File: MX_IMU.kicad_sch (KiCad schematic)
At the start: 31 parts, among them SW1 SW_SPST, U1 ld39150dt33-r, U200 STM32F405RGT6, U4 AT24C256, Y200 16MHz

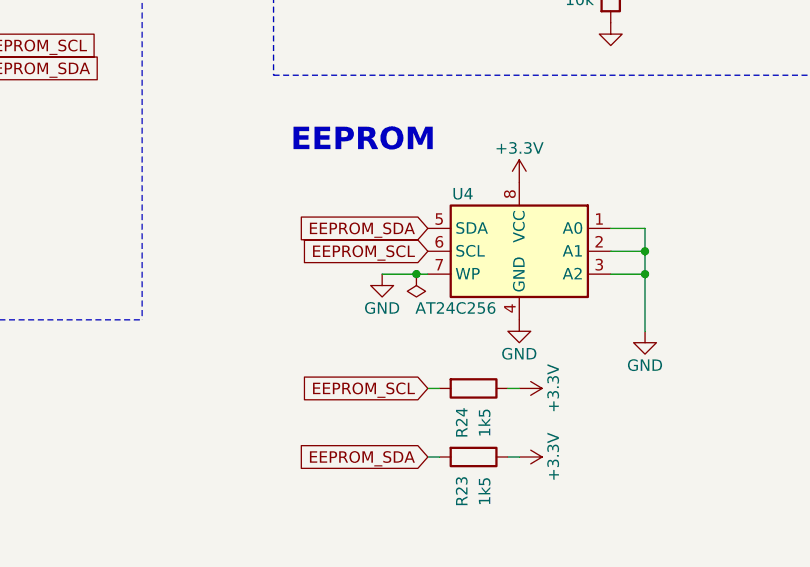
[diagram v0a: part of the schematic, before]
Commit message: add usb and clean up
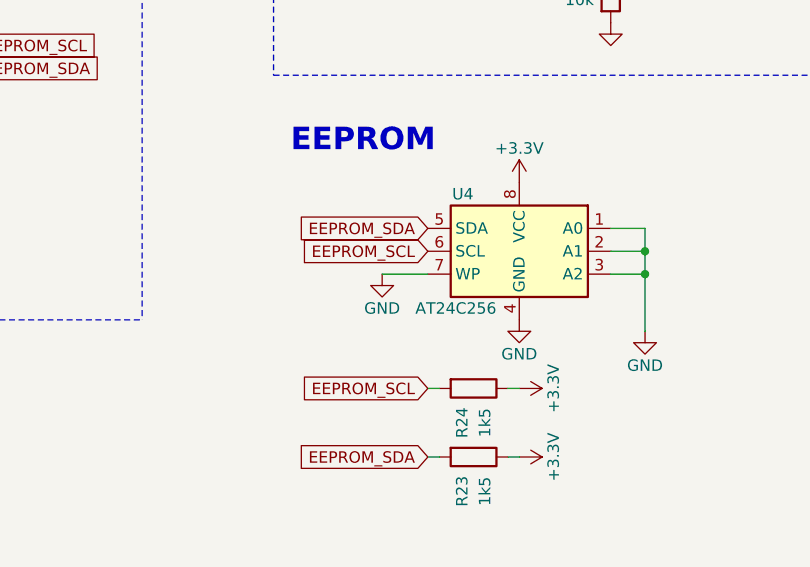
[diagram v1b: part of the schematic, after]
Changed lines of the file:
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@@
 	)
 	(junction
-		(at 151.13 152.4)
-		(diameter 0)
-		(color 0 0 0 0)
-	)
-	(junction
 		(at 69.85 25.4)
 		(diameter 0)
@@
 	(wire
 		(pts
-			(xy 151.13 152.4) (xy 152.4 152.4)
+			(xy 147.32 152.4) (xy 152.4 152.4)
 		)
 		(stroke
@@
 	(wire
 		(pts
-			(xy 147.32 152.4) (xy 151.13 152.4)
-		)
-		(stroke
-			(width 0)
-			(type default)
-		)
-	)
-	(wire
-		(pts
 			(xy 152.4 165.1) (xy 153.67 165.1)
 		)
@@
 			)
 		)
-		(property "Description" ""
+		(property "Description" "Resistor, small symbol"
 			(at 165.1 58.42 0)
 			(effects
@@
 					(size 1.27 1.27)
 				)
+				(hide yes)
 			)
 		)
@@
 					(size 1.27 1.27)
 				)
+				(hide yes)
 			)
 		)
@@
 					(unit 1)
 				)
-			)
-		)
-	)
-	(symbol
-		(lib_id "power:PWR_FLAG")
-		(at 151.13 152.4 180)
-		(unit 1)
-		(exclude_from_sim no)
-		(in_bom yes)
-		(on_board yes)
-		(dnp no)
-		(fields_autoplaced yes)
-		(property "Reference" "#FLG03"
-			(at 151.13 154.305 0)
-			(effects
-				(font
-					(size 1.27 1.27)
-				)
-				(hide yes)
-			)
-		)
-		(property "Value" "PWR_FLAG"
-			(at 151.13 156.972 0)
-			(effects
-				(font
-					(size 1.27 1.27)
-				)
-				(hide yes)
-			)
-		)
-		(property "Footprint" ""
-			(at 151.13 152.4 0)
-			(effects
-				(font
-					(size 1.27 1.27)
-				)
-				(hide yes)
-			)
-		)
-		(property "Datasheet" "~"
-			(at 151.13 152.4 0)
-			(effects
-				(font
-					(size 1.27 1.27)
-				)
-				(hide yes)
-			)
-		)
-		(property "Description" "Special symbol for telling ERC where power comes from"
-			(at 151.13 152.4 0)
-			(effects
-				(font
-					(size 1.27 1.27)
-				)
-				(hide yes)
-			)
-		)
-		(pin "1"
-		)
-		(instances
-			(project ""
-				(path "/8ed38441-7d4e-4e89-870f-07e11c6dce38"
-					(reference "#FLG03")
-					(unit 1)
-				)

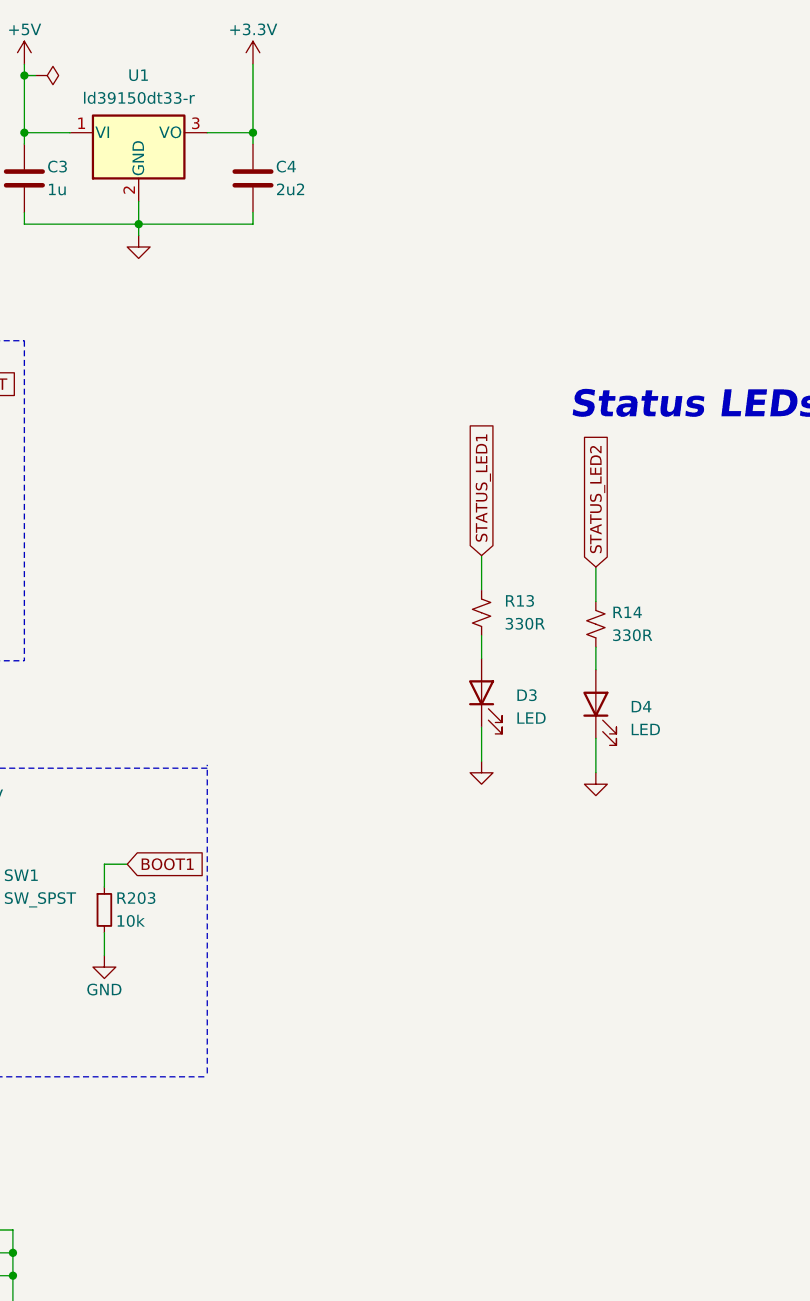
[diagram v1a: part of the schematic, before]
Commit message: add mounting hole
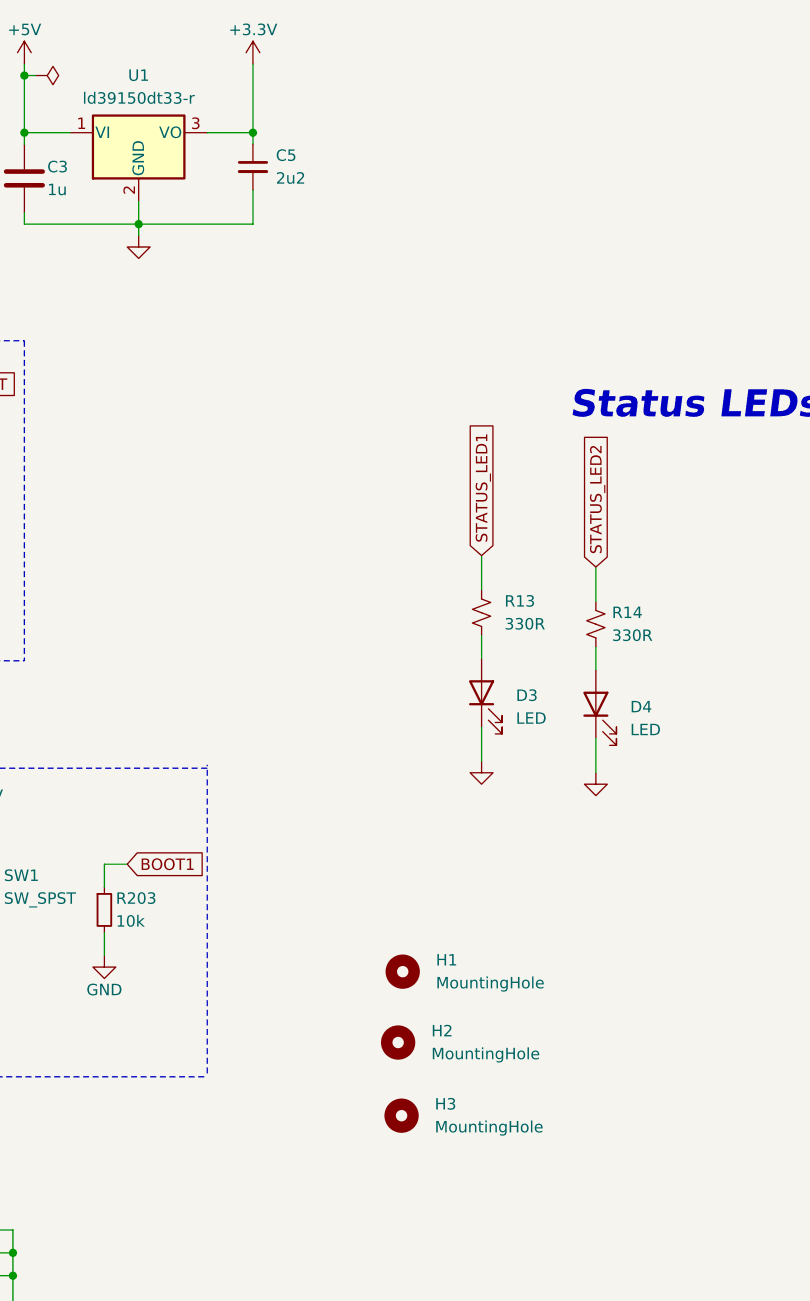
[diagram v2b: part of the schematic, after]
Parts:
- removed C4: 2u2, Capacitor_SMD:C_0603_1608Metric, symbol Device:C
- added C5: 2u2, Capacitor_SMD:C_0603_1608Metric, symbol Device:C_Small
- added H1, H2, H3: MountingHole, MountingHole:MountingHole_2mm, symbol Mechanical:MountingHole
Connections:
- net +3.3V: now also C5.1
- net GND: now also C5.2
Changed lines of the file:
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@@
 	(wire
 		(pts
-			(xy 203.2 35.56) (xy 203.2 34.29)
+			(xy 203.2 31.75) (xy 203.2 35.56)
 		)
 		(stroke
@@
 	)
 	(symbol
-		(lib_id "Device:C")
-		(at 203.2 30.48 0)
+		(lib_id "Mechanical:MountingHole")
+		(at 219.71 134.62 0)
 		(unit 1)
 		(exclude_from_sim no)
-		(in_bom yes)
+		(in_bom no)
 		(on_board yes)
 		(dnp no)
-		(property "Reference" "C4"
-			(at 205.74 29.21 0)
+		(fields_autoplaced yes)
+		(property "Reference" "H3"
+			(at 223.393 133.3499 0)
 			(effects
 				(font
@@
 			)
 		)
-		(property "Value" "2u2"
-			(at 205.74 31.75 0)
+		(property "Value" "MountingHole"
+			(at 223.393 135.8899 0)
 			(effects
 				(font
@@
 			)
 		)
-		(property "Footprint" "Capacitor_SMD:C_0603_1608Metric"
-			(at 204.1652 34.29 0)
+		(property "Footprint" "MountingHole:MountingHole_2mm"
+			(at 219.71 134.62 0)
 			(effects
 				(font
@@
 		)
 		(property "Datasheet" "~"
-			(at 203.2 30.48 0)
+			(at 219.71 134.62 0)
 			(effects
 				(font
@@
 			)
 		)
-		(property "Description" "Unpolarized capacitor"
-			(at 203.2 30.48 0)
+		(property "Description" "Mounting Hole without connection"
+			(at 219.71 134.62 0)
 			(effects
 				(font
@@
 			)
 		)
-		(pin "1"
-		)
-		(pin "2"
-		)
 		(instances
 			(project "MX_IMU"
 				(path "/8ed38441-7d4e-4e89-870f-07e11c6dce38"
-					(reference "C4")
+					(reference "H3")
 					(unit 1)
 				)
@@
 	)
 	(symbol
+		(lib_id "Device:C_Small")
+		(at 203.2 29.21 0)
+		(unit 1)
+		(exclude_from_sim no)
+		(in_bom yes)
+		(on_board yes)
+		(dnp no)
+		(property "Reference" "C5"
+			(at 205.74 27.94 0)
+			(effects
+				(font
+					(size 1.27 1.27)
+				)
+				(justify left)
+			)
+		)
+		(property "Value" "2u2"
+			(at 205.74 30.48 0)
+			(effects
+				(font
+					(size 1.27 1.27)
+				)
+				(justify left)
+			)
+		)
+		(property "Footprint" "Capacitor_SMD:C_0603_1608Metric"
+			(at 203.2 29.21 0)
+			(effects
+				(font
+					(size 1.27 1.27)
+				)
+				(hide yes)
+			)
+		)
+		(property "Datasheet" "~"
+			(at 203.2 29.21 0)
+			(effects
+				(font
+					(size 1.27 1.27)
+				)
+				(hide yes)
+			)
+		)
+		(property "Description" ""
+			(at 203.2 29.21 0)
+			(effects
+				(font
+					(size 1.27 1.27)
+				)
+			)
+		)
+		(property "LCSC Part #" "C23630"
+			(at 203.2 29.21 0)
+			(effects
+				(font
+					(size 1.27 1.27)
+				)
+				(hide yes)
+			)
+		)
+		(pin "1"
+		)
+		(pin "2"
+		)
+		(instances
+			(project "MX_IMU"
+				(path "/8ed38441-7d4e-4e89-870f-07e11c6dce38"
+					(reference "C5")
+					(unit 1)
+				)
+			)
+		)
+	)
+	(symbol
 		(lib_id "power:+3.3V")
 		(at 266.7 63.5 0)
@@
 	)
 	(symbol
+		(lib_id "Mechanical:MountingHole")
+		(at 219.329 126.492 0)
+		(unit 1)
+		(exclude_from_sim no)
+		(in_bom no)
+		(on_board yes)
+		(dnp no)
+		(fields_autoplaced yes)
+		(property "Reference" "H2"
+			(at 223.012 125.2219 0)
+			(effects
+				(font
+					(size 1.27 1.27)
+				)
+				(justify left)
+			)
+		)
+		(property "Value" "MountingHole"
+			(at 223.012 127.7619 0)
+			(effects
+				(font
+					(size 1.27 1.27)
+				)
+				(justify left)
+			)
+		)
+		(property "Footprint" "MountingHole:MountingHole_2mm"
+			(at 219.329 126.492 0)
+			(effects
+				(font
+					(size 1.27 1.27)
+				)
+				(hide yes)
+			)
+		)
+		(property "Datasheet" "~"
+			(at 219.329 126.492 0)
+			(effects
+				(font
+					(size 1.27 1.27)
+				)
+				(hide yes)
+			)
+		)
+		(property "Description" "Mounting Hole without connection"
+			(at 219.329 126.492 0)
+			(effects
+				(font
+					(size 1.27 1.27)
+				)
+				(hide yes)
+			)
+		)
+		(instances
+			(project "MX_IMU"
+				(path "/8ed38441-7d4e-4e89-870f-07e11c6dce38"
+					(reference "H2")
+					(unit 1)
+				)
+			)
+		)
+	)
+	(symbol
 		(lib_id "power:+3.3V")
 		(at 162.56 142.24 0)
@@
 					(unit 1)
 				)
+			)
+		)
+	)
+	(symbol
+		(lib_id "Mechanical:MountingHole")
+		(at 219.837 118.618 0)
+		(unit 1)
+		(exclude_from_sim no)
+		(in_bom no)
+		(on_board yes)
+		(dnp no)
+		(fields_autoplaced yes)
+		(property "Reference" "H1"
+			(at 223.52 117.3479 0)
+			(effects
+				(font
+					(size 1.27 1.27)
+				)
+				(justify left)
+			)
+		)
+		(property "Value" "MountingHole"
+			(at 223.52 119.8879 0)
+			(effects
+				(font
+					(size 1.27 1.27)
+				)
+				(justify left)
+			)
+		)
+		(property "Footprint" "MountingHole:MountingHole_2mm"
+			(at 219.837 118.618 0)
+			(effects
+				(font
+					(size 1.27 1.27)
+				)
+				(hide yes)
+			)
+		)
+		(property "Datasheet" "~"
+			(at 219.837 118.618 0)
+			(effects
+				(font
+					(size 1.27 1.27)
+				)
+				(hide yes)
+			)
+		)
+		(property "Description" "Mounting Hole without connection"
+			(at 219.837 118.618 0)
+			(effects
+				(font
+					(size 1.27 1.27)
+				)
+				(hide yes)
+			)
+		)
+		(instances
+			(project ""
+				(path "/8ed38441-7d4e-4e89-870f-07e11c6dce38"
+					(reference "H1")
+					(unit 1)
+				)

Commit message: Cleanup and check on JCLPCB
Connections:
- net SWO: no longer names the net of U200.55 (PB3)
- no-connect marks 32 -> 33
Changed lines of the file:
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@@
+	)
+	(no_connect
+		(at 104.14 114.3)
 	)
 	(no_connect
@@
 			(effects
 				(font
-					(size 1.27 1.27)
-				)
-				(hide yes)
-			)
-		)
-	)
-	(global_label "SWO"
-		(shape input)
-		(at 104.14 114.3 0)
-		(effects
-			(font
-				(size 1.27 1.27)
-			)
-			(justify left)
-		)
-		(property "Intersheetrefs" "${INTERSHEET_REFS}"
-			(at 104.14 114.3 0)
-			(effects
-				(font
